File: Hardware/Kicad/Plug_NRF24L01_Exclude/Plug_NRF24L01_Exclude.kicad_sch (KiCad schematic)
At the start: 39 parts, among them J1 Conn_01x07_Socket, J2 Conn_01x08_Socket, J2 Conn_02x07_Odd_Even, Q1 2N7002, Q2 2N7002, Q3 2N7002, SW2 SW_SPST, U2 MIC5219-3.3YMM, U3 STM32L412KBTx

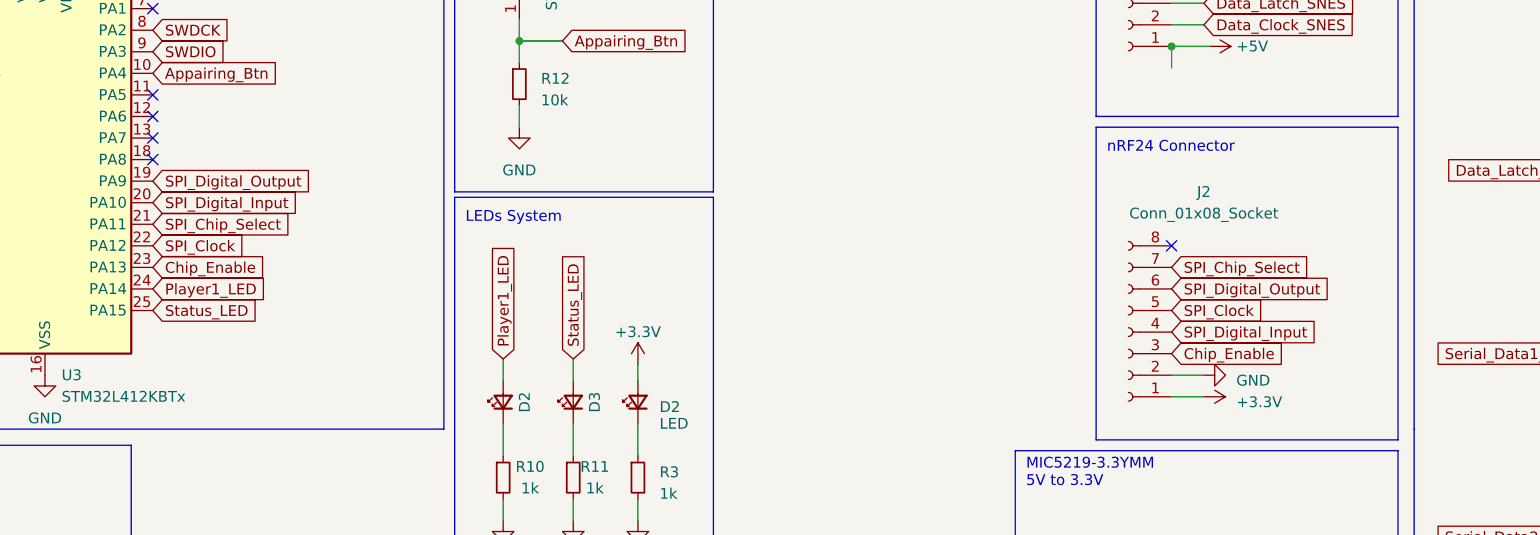
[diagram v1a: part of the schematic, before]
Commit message: Update v2.2a - Plug_NRF24L01_Exclude (SWD_Connector, GND Vias) - Controller_NRF24L01_Exclude (Schematic) - Cleaned Folders
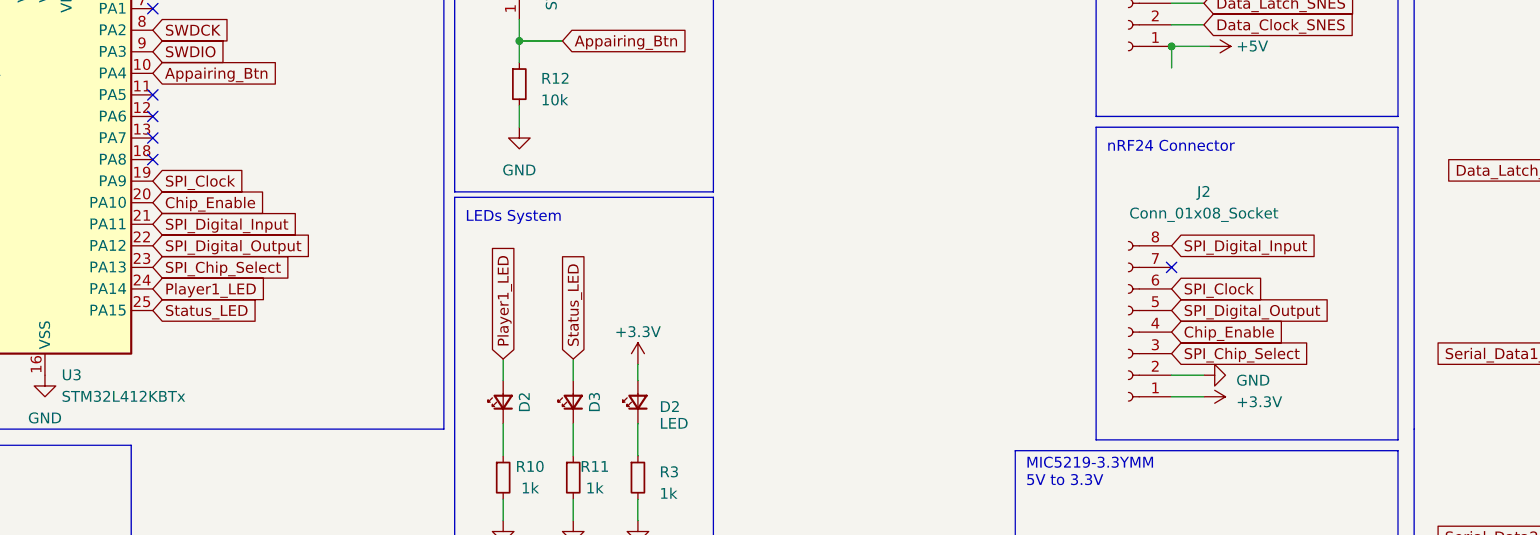
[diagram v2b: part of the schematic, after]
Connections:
- net Chip_Enable: now also J2.4 (Pin_4), U3.20 (PA10); no longer J2.3 (Pin_3), U3.23 (PA13)
- net SPI_Chip_Select: now also J2.3 (Pin_3), U3.23 (PA13); no longer J2.7 (Pin_7), U3.21 (PA11)
- net SPI_Clock: now also J2.6 (Pin_6), U3.19 (PA9); no longer J2.5 (Pin_5), U3.22 (PA12)
- net SPI_Digital_Input: now also J2.8 (Pin_8), U3.21 (PA11); no longer J2.4 (Pin_4), U3.20 (PA10)
- net SPI_Digital_Output: now also J2.5 (Pin_5), U3.22 (PA12); no longer J2.6 (Pin_6), U3.19 (PA9)
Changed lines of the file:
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@@
   (no_connect (at 66.04 39.37))
   (no_connect (at 66.04 57.15))
-  (no_connect (at 186.055 67.31))
   (no_connect (at 49.53 108.585))
   (no_connect (at 49.53 111.125))
@@
   (no_connect (at 36.83 116.205))
   (no_connect (at 40.64 57.15))
+  (no_connect (at 186.055 69.85))
   (no_connect (at 40.64 41.91))
   (no_connect (at 66.04 54.61))
@@
     )
   )
-  (global_label "Chip_Enable" (shape input) (at 186.055 80.01 0) (fields_autoplaced)
-    (effects (font (size 1.27 1.27)) (justify left))
-    (property "Intersheetrefs" "${INTERSHEET_REFS}" (at 200.451 80.01 0)
-      (effects (font (size 1.27 1.27)) (justify left) hide)
-    )
-  )
-  (global_label "SPI_Digital_Output" (shape input) (at 66.04 59.69 0) (fields_autoplaced)
-    (effects (font (size 1.27 1.27)) (justify left))
-    (property "Intersheetrefs" "${INTERSHEET_REFS}" (at 86.3627 59.69 0)
-      (effects (font (size 1.27 1.27)) (justify left) hide)
-    )
-  )
   (global_label "Serial_Data1_STM32" (shape input) (at 40.64 64.77 180) (fields_autoplaced)
     (effects (font (size 1.27 1.27)) (justify right))
@@
     )
   )
+  (global_label "Chip_Enable" (shape input) (at 186.055 77.47 0) (fields_autoplaced)
+    (effects (font (size 1.27 1.27)) (justify left))
+    (property "Intersheetrefs" "${INTERSHEET_REFS}" (at 200.451 77.47 0)
+      (effects (font (size 1.27 1.27)) (justify left) hide)
+    )
+  )
+  (global_label "Chip_Enable" (shape input) (at 66.04 62.23 0) (fields_autoplaced)
+    (effects (font (size 1.27 1.27)) (justify left))
+    (property "Intersheetrefs" "${INTERSHEET_REFS}" (at 80.436 62.23 0)
+      (effects (font (size 1.27 1.27)) (justify left) hide)
+    )
+  )
   (global_label "Data_Clock_STM32" (shape input) (at 237.49 35.56 180) (fields_autoplaced)
     (effects (font (size 1.27 1.27)) (justify right))
@@
     )
   )
-  (global_label "SPI_Digital_Input" (shape input) (at 186.055 77.47 0) (fields_autoplaced)
-    (effects (font (size 1.27 1.27)) (justify left))
-    (property "Intersheetrefs" "${INTERSHEET_REFS}" (at 204.9263 77.47 0)
+  (global_label "SPI_Clock" (shape input) (at 66.04 59.69 0) (fields_autoplaced)
+    (effects (font (size 1.27 1.27)) (justify left))
+    (property "Intersheetrefs" "${INTERSHEET_REFS}" (at 78.1986 59.69 0)
       (effects (font (size 1.27 1.27)) (justify left) hide)
     )
@@
     )
   )
-  (global_label "Chip_Enable" (shape input) (at 66.04 69.85 0) (fields_autoplaced)
-    (effects (font (size 1.27 1.27)) (justify left))
-    (property "Intersheetrefs" "${INTERSHEET_REFS}" (at 80.436 69.85 0)
-      (effects (font (size 1.27 1.27)) (justify left) hide)
-    )
-  )
   (global_label "Data_Clock_STM32" (shape input) (at 40.64 59.69 180) (fields_autoplaced)
     (effects (font (size 1.27 1.27)) (justify right))
@@
     )
   )
+  (global_label "SPI_Digital_Output" (shape input) (at 66.04 67.31 0) (fields_autoplaced)
+    (effects (font (size 1.27 1.27)) (justify left))
+    (property "Intersheetrefs" "${INTERSHEET_REFS}" (at 86.3627 67.31 0)
+      (effects (font (size 1.27 1.27)) (justify left) hide)
+    )
+  )
   (global_label "Serial_Data1_STM32" (shape input) (at 237.49 80.01 180) (fields_autoplaced)
     (effects (font (size 1.27 1.27)) (justify right))
@@
     )
   )
-  (global_label "SPI_Digital_Input" (shape input) (at 66.04 62.23 0) (fields_autoplaced)
-    (effects (font (size 1.27 1.27)) (justify left))
-    (property "Intersheetrefs" "${INTERSHEET_REFS}" (at 84.9113 62.23 0)
-      (effects (font (size 1.27 1.27)) (justify left) hide)
-    )
-  )
   (global_label "Status_LED" (shape input) (at 115.57 80.645 90) (fields_autoplaced)
     (effects (font (size 1.27 1.27)) (justify left))
@@
     )
   )
-  (global_label "SPI_Clock" (shape input) (at 186.055 74.93 0) (fields_autoplaced)
-    (effects (font (size 1.27 1.27)) (justify left))
-    (property "Intersheetrefs" "${INTERSHEET_REFS}" (at 198.2136 74.93 0)
-      (effects (font (size 1.27 1.27)) (justify left) hide)
-    )
-  )
   (global_label "Serial_Data1_SNES" (shape input) (at 189.865 36.195 0) (fields_autoplaced)
     (effects (font (size 1.27 1.27)) (justify left))
@@
     )
   )
-  (global_label "SPI_Chip_Select" (shape input) (at 186.055 69.85 0) (fields_autoplaced)
-    (effects (font (size 1.27 1.27)) (justify left))
-    (property "Intersheetrefs" "${INTERSHEET_REFS}" (at 204.0193 69.85 0)
-      (effects (font (size 1.27 1.27)) (justify left) hide)
-    )
-  )
   (global_label "Serial_Data2_SNES" (shape input) (at 261.62 101.6 0) (fields_autoplaced)
     (effects (font (size 1.27 1.27)) (justify left))
@@
     )
   )
-  (global_label "SPI_Chip_Select" (shape input) (at 66.04 64.77 0) (fields_autoplaced)
-    (effects (font (size 1.27 1.27)) (justify left))
-    (property "Intersheetrefs" "${INTERSHEET_REFS}" (at 84.0043 64.77 0)
-      (effects (font (size 1.27 1.27)) (justify left) hide)
-    )
-  )
-  (global_label "SPI_Clock" (shape input) (at 66.04 67.31 0) (fields_autoplaced)
-    (effects (font (size 1.27 1.27)) (justify left))
-    (property "Intersheetrefs" "${INTERSHEET_REFS}" (at 78.1986 67.31 0)
-      (effects (font (size 1.27 1.27)) (justify left) hide)
-    )
-  )
-  (global_label "SPI_Digital_Output" (shape input) (at 186.055 72.39 0) (fields_autoplaced)
-    (effects (font (size 1.27 1.27)) (justify left))
-    (property "Intersheetrefs" "${INTERSHEET_REFS}" (at 206.3777 72.39 0)
+  (global_label "SPI_Clock" (shape input) (at 186.055 72.39 0) (fields_autoplaced)
+    (effects (font (size 1.27 1.27)) (justify left))
+    (property "Intersheetrefs" "${INTERSHEET_REFS}" (at 198.2136 72.39 0)
       (effects (font (size 1.27 1.27)) (justify left) hide)
     )
@@
     )
   )
+  (global_label "SPI_Digital_Input" (shape input) (at 66.04 64.77 0) (fields_autoplaced)
+    (effects (font (size 1.27 1.27)) (justify left))
+    (property "Intersheetrefs" "${INTERSHEET_REFS}" (at 84.9113 64.77 0)
+      (effects (font (size 1.27 1.27)) (justify left) hide)
+    )
+  )
+  (global_label "SPI_Digital_Input" (shape input) (at 186.055 67.31 0) (fields_autoplaced)
+    (effects (font (size 1.27 1.27)) (justify left))
+    (property "Intersheetrefs" "${INTERSHEET_REFS}" (at 204.9263 67.31 0)
+      (effects (font (size 1.27 1.27)) (justify left) hide)
+    )
+  )
+  (global_label "SPI_Chip_Select" (shape input) (at 186.055 80.01 0) (fields_autoplaced)
+    (effects (font (size 1.27 1.27)) (justify left))
+    (property "Intersheetrefs" "${INTERSHEET_REFS}" (at 204.0193 80.01 0)
+      (effects (font (size 1.27 1.27)) (justify left) hide)
+    )
+  )
   (global_label "Appairing_Btn" (shape input) (at 66.04 46.99 0) (fields_autoplaced)
     (effects (font (size 1.27 1.27)) (justify left))
@@
     )
   )
+  (global_label "SPI_Chip_Select" (shape input) (at 66.04 69.85 0) (fields_autoplaced)
+    (effects (font (size 1.27 1.27)) (justify left))
+    (property "Intersheetrefs" "${INTERSHEET_REFS}" (at 84.0043 69.85 0)
+      (effects (font (size 1.27 1.27)) (justify left) hide)
+    )
+  )
   (global_label "SWDIO" (shape input) (at 49.53 106.045 0) (fields_autoplaced)
     (effects (font (size 1.27 1.27)) (justify left))
@@
       (effects (font (size 1.27 1.27)) (justify left) hide)
     )
+  )
+  (global_label "SPI_Digital_Output" (shape input) (at 186.055 74.93 0) (fields_autoplaced)
+    (effects (font (size 1.27 1.27)) (justify left))
+    (property "Intersheetrefs" "${INTERSHEET_REFS}" (at 206.3777 74.93 0)
+      (effects (font (size 1.27 1.27)) (justify left) hide)
+    )

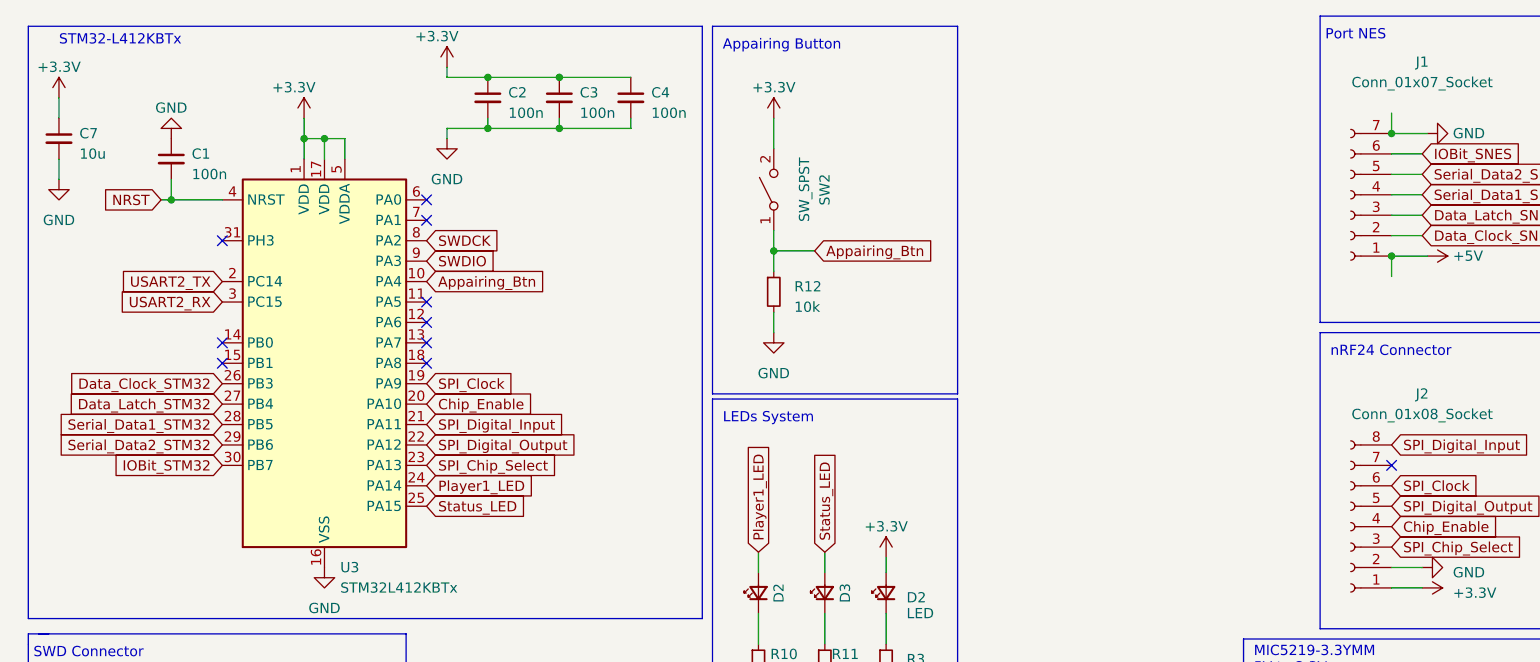
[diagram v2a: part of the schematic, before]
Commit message: Update Plug_NRF24L01 v3.0a (Warnings remaining only)
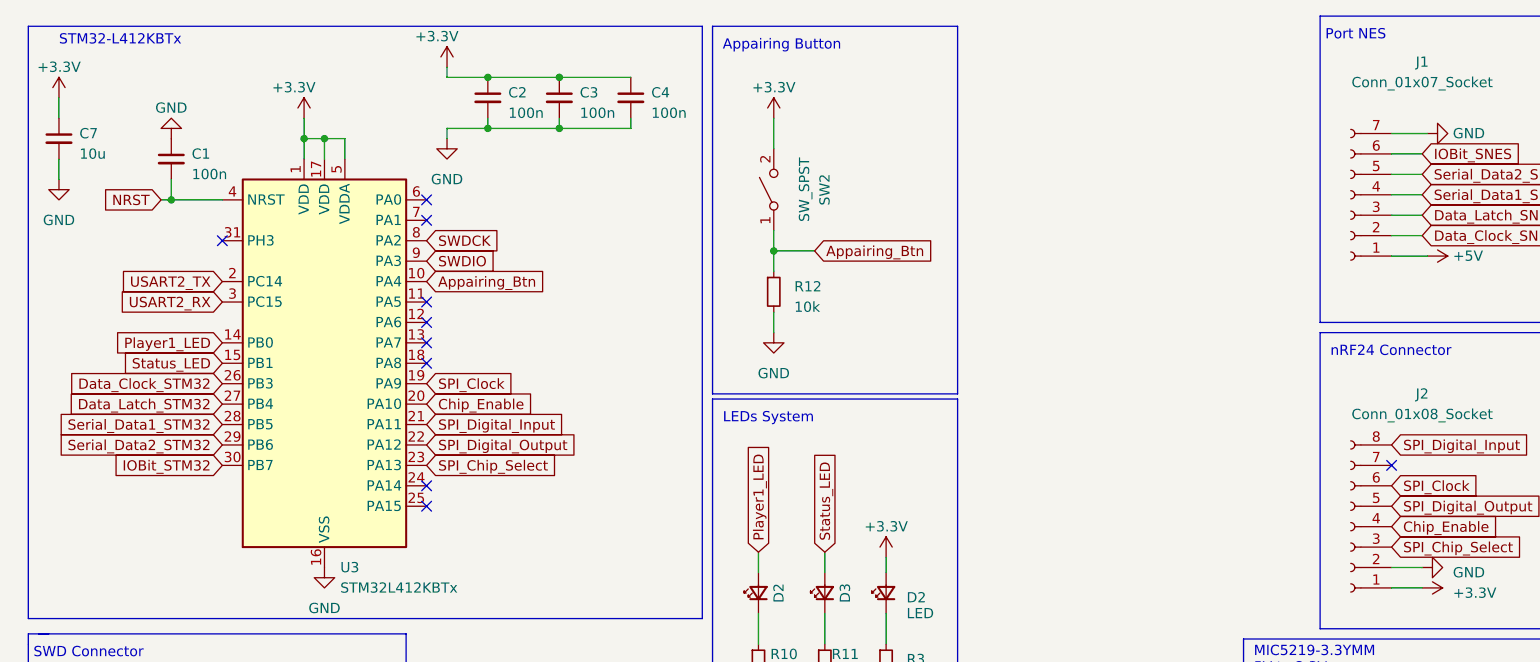
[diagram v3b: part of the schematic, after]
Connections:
- net Player1_LED: now also U3.14 (PB0); no longer U3.24 (PA14)
- net Status_LED: now also U3.15 (PB1); no longer U3.25 (PA15)
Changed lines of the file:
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@@
     (title "SNES Wireless Receiver (NRF24L01 Exclude)")
     (date "2023-04-20")
-    (rev "2.1b")
+    (rev "3.0a")
     (company "ENSEA")
   )
@@
   (junction (at 109.22 43.18) (diameter 0) (color 0 0 0 0)
   )
-  (junction (at 186.055 28.575) (diameter 0) (color 0 0 0 0)
-  )
   (junction (at 259.08 80.01) (diameter 0) (color 0 0 0 0)
   )
@@
   (junction (at 240.03 25.4) (diameter 0) (color 0 0 0 0)
   )
-  (junction (at 186.055 43.815) (diameter 0) (color 0 0 0 0)
-  )
   (junction (at 50.8 29.21) (diameter 0) (color 0 0 0 0)
   )
   (no_connect (at 180.34 113.03))
+  (no_connect (at 66.04 72.39))
   (no_connect (at 36.83 121.285))
   (no_connect (at 66.04 52.07))
   (no_connect (at 66.04 39.37))
+  (no_connect (at 66.04 74.93))
   (no_connect (at 66.04 57.15))
   (no_connect (at 49.53 108.585))
   (no_connect (at 49.53 111.125))
-  (no_connect (at 40.64 54.61))
   (no_connect (at 36.83 116.205))
-  (no_connect (at 40.64 57.15))
   (no_connect (at 186.055 69.85))
   (no_connect (at 40.64 41.91))
@@
     (stroke (width 0) (type default))
   )
-  (wire (pts (xy 186.055 46.355) (xy 186.055 43.815))
-    (stroke (width 0) (type default))
-  )
   (wire (pts (xy 259.08 80.01) (xy 259.08 76.2))
     (stroke (width 0) (type default))
@@
   )
   (wire (pts (xy 186.055 85.09) (xy 189.865 85.09))
-    (stroke (width 0) (type default))
-  )
-  (wire (pts (xy 186.055 26.035) (xy 186.055 28.575))
     (stroke (width 0) (type default))
   )
@@
     )
   )
-  (global_label "Status_LED" (shape input) (at 66.04 74.93 0) (fields_autoplaced)
-    (effects (font (size 1.27 1.27)) (justify left))
-    (property "Intersheetrefs" "${INTERSHEET_REFS}" (at 79.3475 74.93 0)
-      (effects (font (size 1.27 1.27)) (justify left) hide)
-    )
-  )
   (global_label "Data_Latch_STM32" (shape input) (at 237.49 58.42 180) (fields_autoplaced)
     (effects (font (size 1.27 1.27)) (justify right))
@@
     )
   )
-  (global_label "Player1_LED" (shape input) (at 66.04 72.39 0) (fields_autoplaced)
-    (effects (font (size 1.27 1.27)) (justify left))
-    (property "Intersheetrefs" "${INTERSHEET_REFS}" (at 80.4966 72.39 0)
-      (effects (font (size 1.27 1.27)) (justify left) hide)
-    )
-  )
   (global_label "Data_Clock_SNES" (shape input) (at 261.62 35.56 0) (fields_autoplaced)
     (effects (font (size 1.27 1.27)) (justify left))
@@
     )
   )
+  (global_label "Player1_LED" (shape input) (at 40.64 54.61 180) (fields_autoplaced)
+    (effects (font (size 1.27 1.27)) (justify right))
+    (property "Intersheetrefs" "${INTERSHEET_REFS}" (at 26.1834 54.61 0)
+      (effects (font (size 1.27 1.27)) (justify right) hide)
+    )
+  )
   (global_label "Data_Latch_STM32" (shape input) (at 40.64 62.23 180) (fields_autoplaced)
     (effects (font (size 1.27 1.27)) (justify right))
@@
     )
   )
+  (global_label "Status_LED" (shape input) (at 40.64 57.15 180) (fields_autoplaced)
+    (effects (font (size 1.27 1.27)) (justify right))
+    (property "Intersheetrefs" "${INTERSHEET_REFS}" (at 27.3325 57.15 0)
+      (effects (font (size 1.27 1.27)) (justify right) hide)
+    )
+  )
   (global_label "SPI_Chip_Select" (shape input) (at 66.04 69.85 0) (fields_autoplaced)
     (effects (font (size 1.27 1.27)) (justify left))
@@
     )
   )
-  (netclass_flag "" (length 2.54) (shape round) (at 186.055 46.355 270)
-    (effects (font (size 1.27 1.27)) (justify right bottom))
-    (property "Netclass" "SNES" (at 195.58 46.355 0)
-      (effects (font (size 1.27 1.27) italic) (justify right))
-    )
-  )
-  (netclass_flag "" (length 2.54) (shape round) (at 186.055 26.035 270)
-    (effects (font (size 1.27 1.27)) (justify right bottom))
-    (property "Netclass" "SNES" (at 195.58 26.035 0)
-      (effects (font (size 1.27 1.27) italic) (justify right))
-    )
-  )
